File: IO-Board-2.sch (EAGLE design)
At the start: 143 parts, among them J1.1 TPPAD1-13, J1.2 TPPAD1-13, J1.3 TPPAD1-13, J1.4 TPPAD1-13, J1.5 TPPAD1-13, J1.6 TPPAD1-13, J1.7 TPPAD1-13, J1.8 TPPAD1-13, J2.1 TPPAD1-13, J2.2 TPPAD1-13, J2.3 TPPAD1-13, J2.4 TPPAD1-13, J2.5 TPPAD1-13, J2.6 TPPAD1-13, J2.7 TPPAD1-13, J2.8 TPPAD1-13, J3.1 TPPAD1-13, J3.2 TPPAD1-13, J3.3 TPPAD1-13, J3.4 TPPAD1-13, J3.5 TPPAD1-13, J3.6 TPPAD1-13, J3.7 TPPAD1-13, J3.8 TPPAD1-13, J4.5 TPPAD1-13, J4.6 TPPAD1-13, J4.7 TPPAD1-13, J4.8 TPPAD1-13

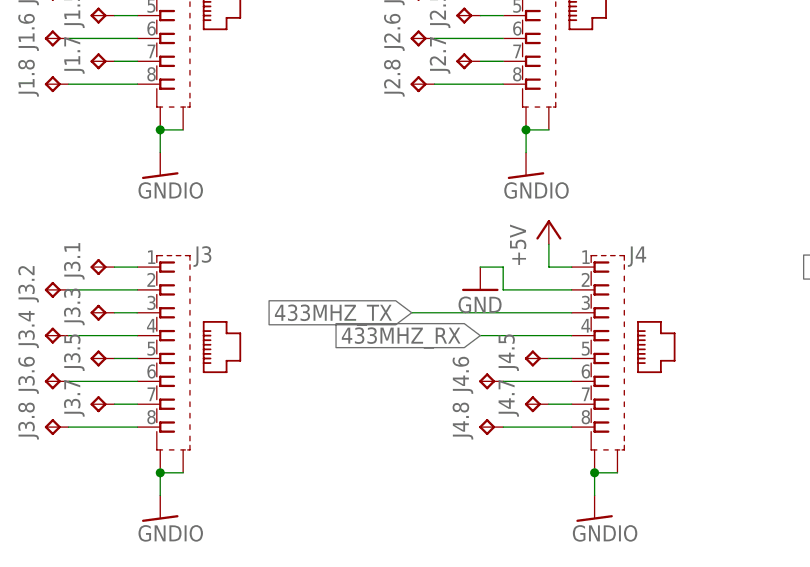
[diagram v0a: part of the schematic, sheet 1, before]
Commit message: 433MHz-Server und IO-Board-2 Anpassungen
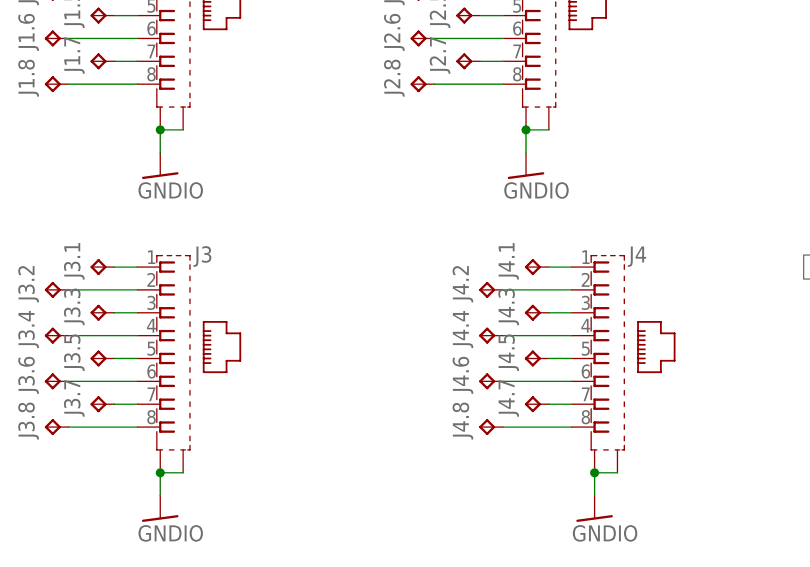
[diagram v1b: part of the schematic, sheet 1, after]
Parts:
- added 433_RX, 433_TX, J4.1, J4.2, J4.3, J4.4: TPPAD1-13, testpad:TPPAD1-13
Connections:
- new net N$1: J4.4, J4.4.TP
- new net N$3: J4.3, J4.3.TP
- new net N$4: J4.2, J4.2.TP
- new net N$5: J4.1, J4.1.TP
- net +5V: no longer J4.1
- net 433MHZ_RX: now also 433_RX.TP; no longer J4.4
- net 433MHZ_TX: now also 433_TX.TP; no longer J4.3
- net GND: no longer J4.2
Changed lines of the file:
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@@
 <part name="GND2" library="supply1" deviceset="GND" device=""/>
 <part name="P+1" library="supply1" deviceset="+5V" device=""/>
-<part name="P+2" library="supply1" deviceset="+5V" device=""/>
-<part name="GND3" library="supply1" deviceset="GND" device=""/>
 <part name="1WIRE.5" library="testpad" deviceset="TP" device="PAD1-13" value="TPPAD1-13"/>
 <part name="+3V3.5" library="testpad" deviceset="TP" device="PAD1-13" value="TPPAD1-13"/>
@@
 <part name="P+5" library="supply1" deviceset="+5V" device=""/>
 <part name="GND7" library="supply1" deviceset="GND" device=""/>
+<part name="J4.1" library="testpad" deviceset="TP" device="PAD1-13" value="TPPAD1-13"/>
+<part name="J4.2" library="testpad" deviceset="TP" device="PAD1-13" value="TPPAD1-13"/>
+<part name="J4.3" library="testpad" deviceset="TP" device="PAD1-13" value="TPPAD1-13"/>
+<part name="J4.4" library="testpad" deviceset="TP" device="PAD1-13" value="TPPAD1-13"/>
+<part name="433_TX" library="testpad" deviceset="TP" device="PAD1-13" value="TPPAD1-13"/>
+<part name="433_RX" library="testpad" deviceset="TP" device="PAD1-13" value="TPPAD1-13"/>
 </parts>
 <sheets>
@@
 <instance part="GND2" gate="1" x="50.8" y="45.72"/>
 <instance part="P+1" gate="1" x="66.04" y="12.7"/>
-<instance part="P+2" gate="1" x="144.78" y="50.8"/>
-<instance part="GND3" gate="1" x="137.16" y="43.18"/>
 <instance part="1WIRE.5" gate="G$1" x="236.22" y="48.26"/>
 <instance part="+3V3.5" gate="G$1" x="236.22" y="38.1"/>
@@
 <instance part="P+3" gate="1" x="248.92" y="40.64"/>
 <instance part="GND4" gate="1" x="45.72" y="78.74"/>
+<instance part="J4.1" gate="G$1" x="142.24" y="45.72" rot="R90"/>
+<instance part="J4.2" gate="G$1" x="137.16" y="43.18" rot="R90"/>
+<instance part="J4.3" gate="G$1" x="142.24" y="40.64" rot="R90"/>
+<instance part="J4.4" gate="G$1" x="137.16" y="38.1" rot="R90"/>
 </instances>
 <busses>
@@
 <junction x="185.42" y="17.78"/>
 <junction x="180.34" y="17.78"/>
-</segment>
-<segment>
-<pinref part="J4" gate="G$1" pin="2"/>
-<wire x1="147.32" y1="43.18" x2="139.7" y2="43.18" width="0.1524" layer="91"/>
-<wire x1="139.7" y1="43.18" x2="139.7" y2="45.72" width="0.1524" layer="91"/>
-<pinref part="GND3" gate="1" pin="GND"/>
-<wire x1="139.7" y1="45.72" x2="137.16" y2="45.72" width="0.1524" layer="91"/>
 </segment>
 </net>
@@
 <label x="58.42" y="71.12" size="1.778" layer="95" xref="yes"/>
 </segment>
-<segment>
-<pinref part="J4" gate="G$1" pin="3"/>
-<wire x1="147.32" y1="40.64" x2="129.54" y2="40.64" width="0.1524" layer="91"/>
-<label x="129.54" y="40.64" size="1.778" layer="95" rot="R180" xref="yes"/>
-</segment>
 </net>
 <net name="N$2" class="0">
@@
 <label x="66.04" y="63.5" size="1.778" layer="95" xref="yes"/>
 </segment>
-<segment>
-<pinref part="J4" gate="G$1" pin="4"/>
-<wire x1="147.32" y1="38.1" x2="137.16" y2="38.1" width="0.1524" layer="91"/>
-<label x="137.16" y="38.1" size="1.778" layer="95" rot="R180" xref="yes"/>
-</segment>
 </net>
 <net name="+5V" class="0">
@@
 <wire x1="20.32" y1="5.08" x2="66.04" y2="5.08" width="0.1524" layer="91"/>
 <wire x1="66.04" y1="5.08" x2="66.04" y2="10.16" width="0.1524" layer="91"/>
-</segment>
-<segment>
-<pinref part="J4" gate="G$1" pin="1"/>
-<pinref part="P+2" gate="1" pin="+5V"/>
-<wire x1="147.32" y1="45.72" x2="144.78" y2="45.72" width="0.1524" layer="91"/>
-<wire x1="144.78" y1="45.72" x2="144.78" y2="48.26" width="0.1524" layer="91"/>
 </segment>
 <segment>
@@
 </segment>
 </net>
+<net name="N$1" class="0">
+<segment>
+<pinref part="J4.4" gate="G$1" pin="TP"/>
+<pinref part="J4" gate="G$1" pin="4"/>
+<wire x1="139.7" y1="38.1" x2="147.32" y2="38.1" width="0.1524" layer="91"/>
+</segment>
+</net>
+<net name="N$3" class="0">
+<segment>
+<pinref part="J4" gate="G$1" pin="3"/>
+<pinref part="J4.3" gate="G$1" pin="TP"/>
+<wire x1="147.32" y1="40.64" x2="144.78" y2="40.64" width="0.1524" layer="91"/>
+</segment>
+</net>
+<net name="N$4" class="0">
+<segment>
+<pinref part="J4.2" gate="G$1" pin="TP"/>
+<pinref part="J4" gate="G$1" pin="2"/>
+<wire x1="139.7" y1="43.18" x2="147.32" y2="43.18" width="0.1524" layer="91"/>
+</segment>
+</net>
+<net name="N$5" class="0">
+<segment>
+<pinref part="J4.1" gate="G$1" pin="TP"/>
+<pinref part="J4" gate="G$1" pin="1"/>
+<wire x1="144.78" y1="45.72" x2="147.32" y2="45.72" width="0.1524" layer="91"/>
+</segment>
+</net>
 </nets>
 </sheet>
@@
 <instance part="P+5" gate="1" x="73.66" y="68.58"/>
 <instance part="GND7" gate="1" x="93.98" y="50.8"/>
+<instance part="433_TX" gate="G$1" x="25.4" y="66.04"/>
+<instance part="433_RX" gate="G$1" x="83.82" y="58.42"/>
 </instances>
 <busses>
@@
 <pinref part="JP1" gate="1" pin="1"/>
 <wire x1="38.1" y1="63.5" x2="38.1" y2="60.96" width="0.1524" layer="91"/>
-<wire x1="38.1" y1="60.96" x2="30.48" y2="60.96" width="0.1524" layer="91"/>
-<label x="30.48" y="60.96" size="1.778" layer="95" rot="R180" xref="yes"/>
+<wire x1="38.1" y1="60.96" x2="25.4" y2="60.96" width="0.1524" layer="91"/>
+<label x="22.86" y="60.96" size="1.778" layer="95" rot="R180" xref="yes"/>
+<pinref part="433_TX" gate="G$1" pin="TP"/>
+<wire x1="25.4" y1="60.96" x2="22.86" y2="60.96" width="0.1524" layer="91"/>
+<wire x1="25.4" y1="63.5" x2="25.4" y2="60.96" width="0.1524" layer="91"/>
+<junction x="25.4" y="60.96"/>
 </segment>
 </net>
@@
 <segment>
 <pinref part="JP2" gate="G$1" pin="3"/>
-<wire x1="91.44" y1="66.04" x2="91.44" y2="58.42" width="0.1524" layer="91"/>
-<wire x1="91.44" y1="58.42" x2="81.28" y2="58.42" width="0.1524" layer="91"/>
-<label x="81.28" y="58.42" size="1.778" layer="95" rot="R180" xref="yes"/>
-</segment>
-</net>
+<wire x1="91.44" y1="66.04" x2="91.44" y2="53.34" width="0.1524" layer="91"/>
+<wire x1="91.44" y1="53.34" x2="83.82" y2="53.34" width="0.1524" layer="91"/>
+<label x="81.28" y="53.34" size="1.778" layer="95" rot="R180" xref="yes"/>
+<pinref part="433_RX" gate="G$1" pin="TP"/>
+<wire x1="83.82" y1="53.34" x2="81.28" y2="53.34" width="0.1524" layer="91"/>
+<wire x1="83.82" y1="55.88" x2="83.82" y2="53.34" width="0.1524" layer="91"/>
+<junction x="83.82" y="53.34"/>
+</segment>
+</net>

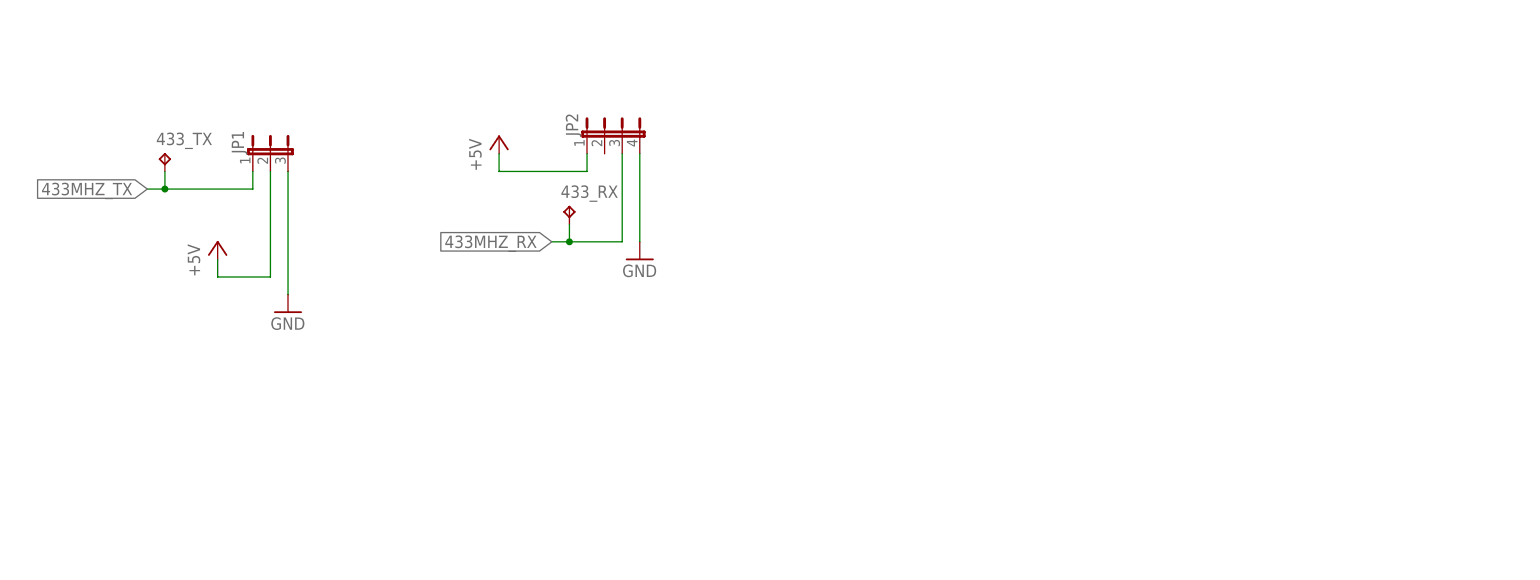
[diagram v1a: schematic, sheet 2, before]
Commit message: IO-Board und IO-Board-2 Anpassungen
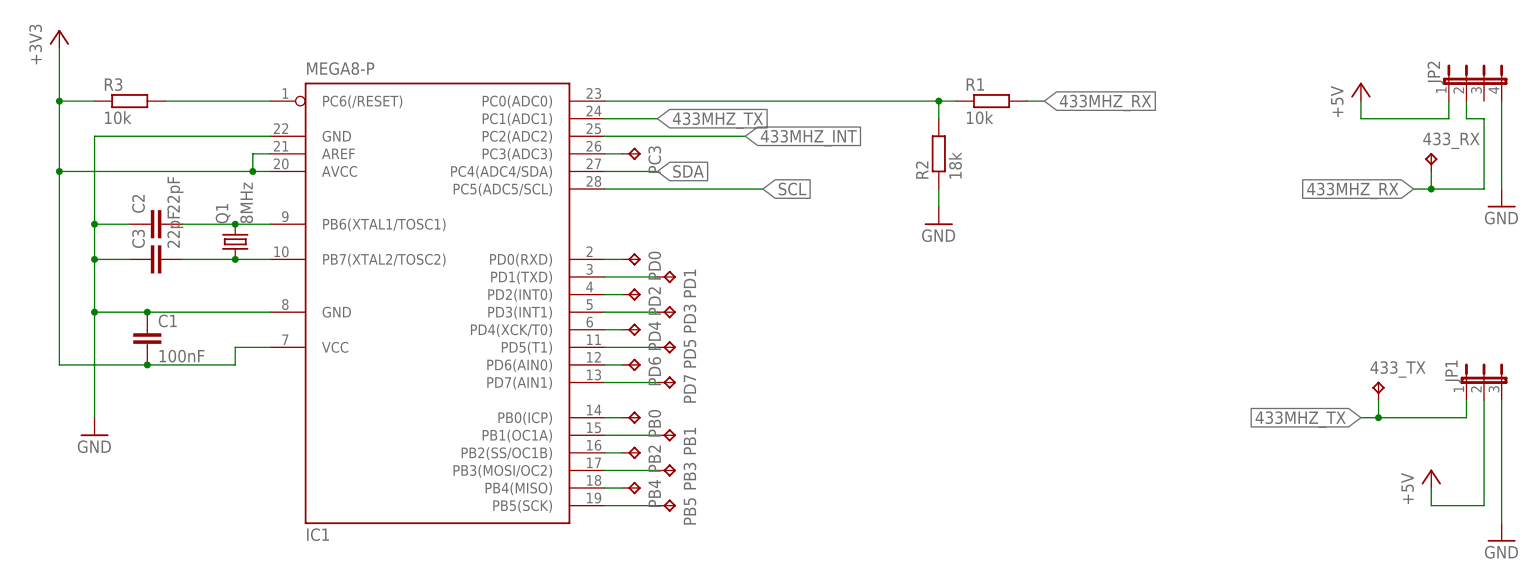
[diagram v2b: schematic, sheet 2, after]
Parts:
- added C1: 100nF, rcl:C-EU025-025X050
- added C2, C3: 22pF, rcl:C-EU025-025X050
- added GPIO_24, PB0, PB1, PB2, PB3, PB4, PB5, PC3, PD0, PD1, PD2, PD3, PD4, PD5, PD6, PD7: TPPAD1-13, testpad:TPPAD1-13
- added IC1: MEGA8-P, atmel:MEGA8-P
- added Q1: 8MHz, crystal:CRYSTALHC49U-V
- added R3: 10k, rcl:R-EU_0204/2V
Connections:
- removed net GND.2: R2.1, SV1.29
- new net +5V_2: JP1.2, JP2.1, SV1.28
- new net 433MHZ_INT: IC1.PC2(ADC2), SV1.27
- new net GND_2: JP1.3, JP2.4, R2.1, SV1.29
- new net N$10: IC1.PD1(TXD), PD1.TP
- new net N$11: IC1.PD2(INT0), PD2.TP
- new net N$12: IC1.PD3(INT1), PD3.TP
- new net N$13: IC1.PD4(XCK/T0), PD4.TP
- new net N$14: IC1.PD5(T1), PD5.TP
- new net N$15: IC1.PD6(AIN0), PD6.TP
- new net N$16: IC1.PD7(AIN1), PD7.TP
- new net N$17: IC1.PB0(ICP), PB0.TP
- new net N$18: IC1.PB1(OC1A), PB1.TP
- new net N$19: IC1.PB2(SS/OC1B), PB2.TP
- new net N$20: IC1.PB3(MOSI/OC2), PB3.TP
- new net N$21: IC1.PB4(MISO), PB4.TP
- new net N$22: IC1.PB5(SCK), PB5.TP
- new net N$23: C3.2, IC1.PB7(XTAL2/TOSC2), Q1.1
- new net N$24: C2.2, IC1.PB6(XTAL1/TOSC1), Q1.2
- new net N$6: IC1.PC6(/RESET), R3.2
- new net N$7: GPIO_24.TP, SV1.26
- new net N$8: IC1.PC3(ADC3), PC3.TP
- new net N$9: IC1.PD0(RXD), PD0.TP
- net +3V3: now also C1.2, IC1.AREF, IC1.AVCC, IC1.VCC@1, R3.1
- net +5V: no longer JP1.2, JP2.1
- net 433MHZ_RX: now also JP2.2; no longer JP2.3
- net 433MHZ_TX: now also IC1.PC1(ADC1); no longer SV1.27
- net GND: now also C1.1, C2.1, C3.1, IC1.GND, IC1.GND@1; no longer JP1.3, JP2.4
- net N$2: now also IC1.PC0(ADC0); no longer SV1.26
- net SCL: now also IC1.PC5(ADC5/SCL)
- net SDA: now also IC1.PC4(ADC4/SDA)
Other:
- moved on the sheet: 433_RX, 433_TX, JP1, JP2

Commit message: IO-Board-2 Anpassung
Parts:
- R1, R2: device rcl:R-EU_0204/2V -> rcl:R-EU_0204/5
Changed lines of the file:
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@@
 <part name="VCCIO.23" library="testpad" deviceset="TP" device="PAD1-13" value="TPPAD1-13"/>
 <part name="VCCIO.24" library="testpad" deviceset="TP" device="PAD1-13" value="TPPAD1-13"/>
-<part name="R1" library="rcl" deviceset="R-EU_" device="0204/2V" value="10k"/>
-<part name="R2" library="rcl" deviceset="R-EU_" device="0204/2V" value="18k"/>
+<part name="R1" library="rcl" deviceset="R-EU_" device="0204/5" value="10k"/>
+<part name="R2" library="rcl" deviceset="R-EU_" device="0204/5" value="18k"/>
 <part name="P+1" library="supply1" deviceset="+5V" device=""/>
 <part name="1WIRE.5" library="testpad" deviceset="TP" device="PAD1-13" value="TPPAD1-13"/>
